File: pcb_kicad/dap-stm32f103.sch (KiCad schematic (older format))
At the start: 4 parts

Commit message: [update] pcb
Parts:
- added C?: 0402_100nF__104_10%_16V, lc_lib:0402_C, symbol lc_Cap:0402_100nF__104_10%_16V
- added R?: 0402_10KΩ__1002_1%, lc_lib:0402_R, symbol lc_RES:0402_10KΩ__1002_1%
- added R?: 0402_100KΩ__1003_1%, lc_lib:0402_R, symbol lc_RES:0402_100KΩ__1003_1%
- added R? (x2): 0402_4.7KΩ__4701_1%, lc_lib:0402_R, symbol lc_RES:0402_4.7KΩ__4701_1%
- added U? (x2): STM32F103CBT6, lc_lib:LQFP-48_7X7X05P, symbol lc_MCU:STM32F103CBT6
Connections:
- net labels added: +3.3V
- wire segments 9 -> 21
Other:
- moved on the sheet: C?, Y?

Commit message: [update] pcb sch
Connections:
- wire segments 21 -> 29
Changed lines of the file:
@@
 P 3800 2700
 F 0 "U?" H 3750 1111 50  0000 C CNN
-F 1 "STM32F103CBTx" H 3750 1020 50  0000 C CNN
+F 1 "STM32F103CBTx" H 3500 1000 50  0000 C CNN
 F 2 "Package_QFP:LQFP-48_7x7mm_P0.5mm" H 3200 1300 50  0001 R CNN
 F 3 "http://www.st.com/st-web-ui/static/active/en/resource/technical/document/datasheet/CD00161566.pdf" H 3800 2700 50  0001 C CNN
@@
 Wire Wire Line
 	5250 2950 5250 3050
+$Comp
+L power:GND #PWR?
+U 1 1 5D9F8DE0
+P 3900 4500
+F 0 "#PWR?" H 3900 4250 50  0001 C CNN
+F 1 "GND" H 3905 4327 50  0000 C CNN
+F 2 "" H 3900 4500 50  0001 C CNN
+F 3 "" H 3900 4500 50  0001 C CNN
+	1    3900 4500
+	1    0    0    -1
+$EndComp
+Wire Wire Line
+	3900 4500 3900 4200
+Wire Wire Line
+	3900 4200 3800 4200
+Connection ~ 3900 4200
+Connection ~ 3700 4200
+Wire Wire Line
+	3700 4200 3600 4200
+Connection ~ 3800 4200
+Wire Wire Line
+	3800 4200 3700 4200
+Wire Wire Line
+	3600 1200 3700 1200
+Connection ~ 3600 1200
+Connection ~ 3700 1200
+Wire Wire Line
+	3700 1200 3800 1200
+Connection ~ 3800 1200
+Wire Wire Line
+	3800 1200 3900 1200
+Connection ~ 3900 1200
+Wire Wire Line
+	3900 1200 4000 1200
 $EndSCHEMATC

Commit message: [update] SCH
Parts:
- removed U? (x2): STM32F103CBT6, lc_lib:LQFP-48_7X7X05P, symbol lc_MCU:STM32F103CBT6
- added C? (x2): 0402_18pF__180_5%_50V, lc_lib:0402_C, symbol lc_Cap:0402_18pF__180_5%_50V
- added C? (x2): 0402_100nF__104_10%_16V, lc_lib:0402_C, symbol lc_Cap:0402_100nF__104_10%_16V
- added C? (x2): 0603_10uF__106_10%_10V, lc_lib:0603_C, symbol lc_Cap:0603_10uF__106_10%_10V
- added D_BULE: 0603_蓝灯, lc_lib:0603_LED_S1, symbol lc_LED:0603_蓝灯
- added D_GREEN: 0603_绿灯, lc_lib:0603_LED_S1, symbol lc_LED:0603_绿灯
- added D_RED: 0603_红灯, lc_lib:0603_LED_S1, symbol lc_LED:0603_红灯
- added J?: USB_C_Receptacle_USB2.0, Connector_USB:USB_C_Receptacle_Palconn_UTC16-G, symbol Connector:USB_C_Receptacle_USB2.0
- added R? (x3): 0402_470Ω__4700_1%, lc_lib:0402_R, symbol lc_RES:0402_470Ω__4700_1%
- added R?: 0402_100Ω__1000_1%, lc_lib:0402_R, symbol lc_RES:0402_100Ω__1000_1%
- added R?: 0402_100KΩ__1003_1%, lc_lib:0402_R, symbol lc_RES:0402_100KΩ__1003_1%
- added R? (x2): 0402_33Ω__33R0_1%, lc_lib:0402_R, symbol lc_RES:0402_33Ω__33R0_1%
- added SWD/JTAG: Conn_02x05_Top_Bottom, Connector_PinHeader_2.54mm:PinHeader_2x05_P2.54mm_Vertical, symbol Connector_Generic:Conn_02x05_Top_Bottom
- added VR?: SOT-223_AMS1117-3.3, lc_lib:SOT-223, symbol lc_LDO:SOT-223_AMS1117-3.3
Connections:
- net labels added: LED_BULE, LED_GREEN, LED_RED, TGT_NRESET, TGT_RX, TGT_SWCLK, TGT_SWDIO, TGT_SWO, TGT_TX, TGT_USB_D+, TGT_USB_D-
- wire segments 29 -> 96
- no-connect marks 0 -> 5

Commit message: [update] SCH done
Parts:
- added C11, C12, C13, C14, C4: 0402_100nF__104_10%_16V, lc_lib:0402_C, symbol lc_Cap:0402_100nF__104_10%_16V
- added IF_SWD1: Conn_01x05, Connector_PinHeader_2.54mm:PinHeader_1x05_P2.54mm_Vertical, symbol Connector_Generic:Conn_01x05
- added R1: 0402_10KΩ__1002_1%, lc_lib:0402_R, symbol lc_RES:0402_10KΩ__1002_1%
- gave numbers to parts that had none: 24
- renumbered D_BULE to D_BULE1, D_GREEN to D_GREEN1, D_RED to D_RED1, SWD/JTAG to SWD/JTAG1
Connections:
- net +3V3: now also C11.1, C12.1, C13.1, C14.1, IF_SWD1.5 (Pin_5), R1.1
- net GND: now also U1.20 (PB2), C11.2, C12.2, C13.2, C14.2, C4.2, IF_SWD1.2 (Pin_2)
- net TGT_NRESET: now also U1.18 (PB0), C4.1, R1.2
- net TGT_RX: now also U1.12 (PA2)
- net IF_SWDIO: now reaches U1.34 (PA13)
- net IF_SWDIO: now also IF_SWD1.4 (Pin_4)
- net IF_SWCLK: now reaches U1.37 (PA14)
- net IF_SWCLK: now also IF_SWD1.3 (Pin_3)
- net IF_NRESET: now reaches C3.2, R8.2, U1.7 (NRST)
- net IF_NRESET: now also IF_SWD1.1 (Pin_1)
- no-connect marks 5 -> 22
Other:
- moved on the sheet: C3

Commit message: [update] pcb
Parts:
- added JTAG1: Conn_02x10_Top_Bottom, Connector_PinHeader_2.54mm:PinHeader_2x10_P2.54mm_Vertical, symbol Connector_Generic:Conn_02x10_Top_Bottom
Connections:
- net +3V3: now also JTAG1.1 (Pin_1), JTAG1.11 (Pin_11)
- net GND: now also JTAG1.12 (Pin_12), JTAG1.13 (Pin_13), JTAG1.14 (Pin_14), JTAG1.15 (Pin_15), JTAG1.16 (Pin_16), JTAG1.17 (Pin_17), JTAG1.18 (Pin_18), JTAG1.19 (Pin_19), JTAG1.20 (Pin_20)
- net TGT_NRESET: now also JTAG1.2 (Pin_2), JTAG1.8 (Pin_8)
- net TGT_RX: now also JTAG1.3 (Pin_3)
- net TGT_SWCLK: now also JTAG1.5 (Pin_5)
- net TGT_SWDIO: now also JTAG1.4 (Pin_4)
- net TGT_SWO: now also JTAG1.7 (Pin_7)
- no-connect marks 22 -> 25
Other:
- moved on the sheet: C11, C12, C13, C14, IF_SWD1, SWD/JTAG1

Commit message: [update] pcb 连线完成
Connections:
- net GND: now also J1.S1 (SHIELD)
- net TGT_NRESET: no longer JTAG1.2 (Pin_2)
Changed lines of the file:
@@
 NoConn ~ 4200 6750
 NoConn ~ 4200 6850
-NoConn ~ 3300 7150
 NoConn ~ 4200 5850
 NoConn ~ 4200 5950
@@
 Wire Wire Line
 	8800 4750 8850 4750
-Text Label 8400 4850 0    50   ~ 0
-TGT_NRESET
 Text Label 8400 4950 0    50   ~ 0
 TGT_RX
@@
 NoConn ~ 8850 5650
 Wire Wire Line
-	8400 4850 8850 4850
-Wire Wire Line
 	8400 4950 8850 4950
 Wire Wire Line
@@
 	8850 5450 8400 5450
 NoConn ~ 8850 5250
+NoConn ~ 8850 4850
+Wire Wire Line
+	3300 7150 3600 7150
+Connection ~ 3600 7150
 $EndSCHEMATC

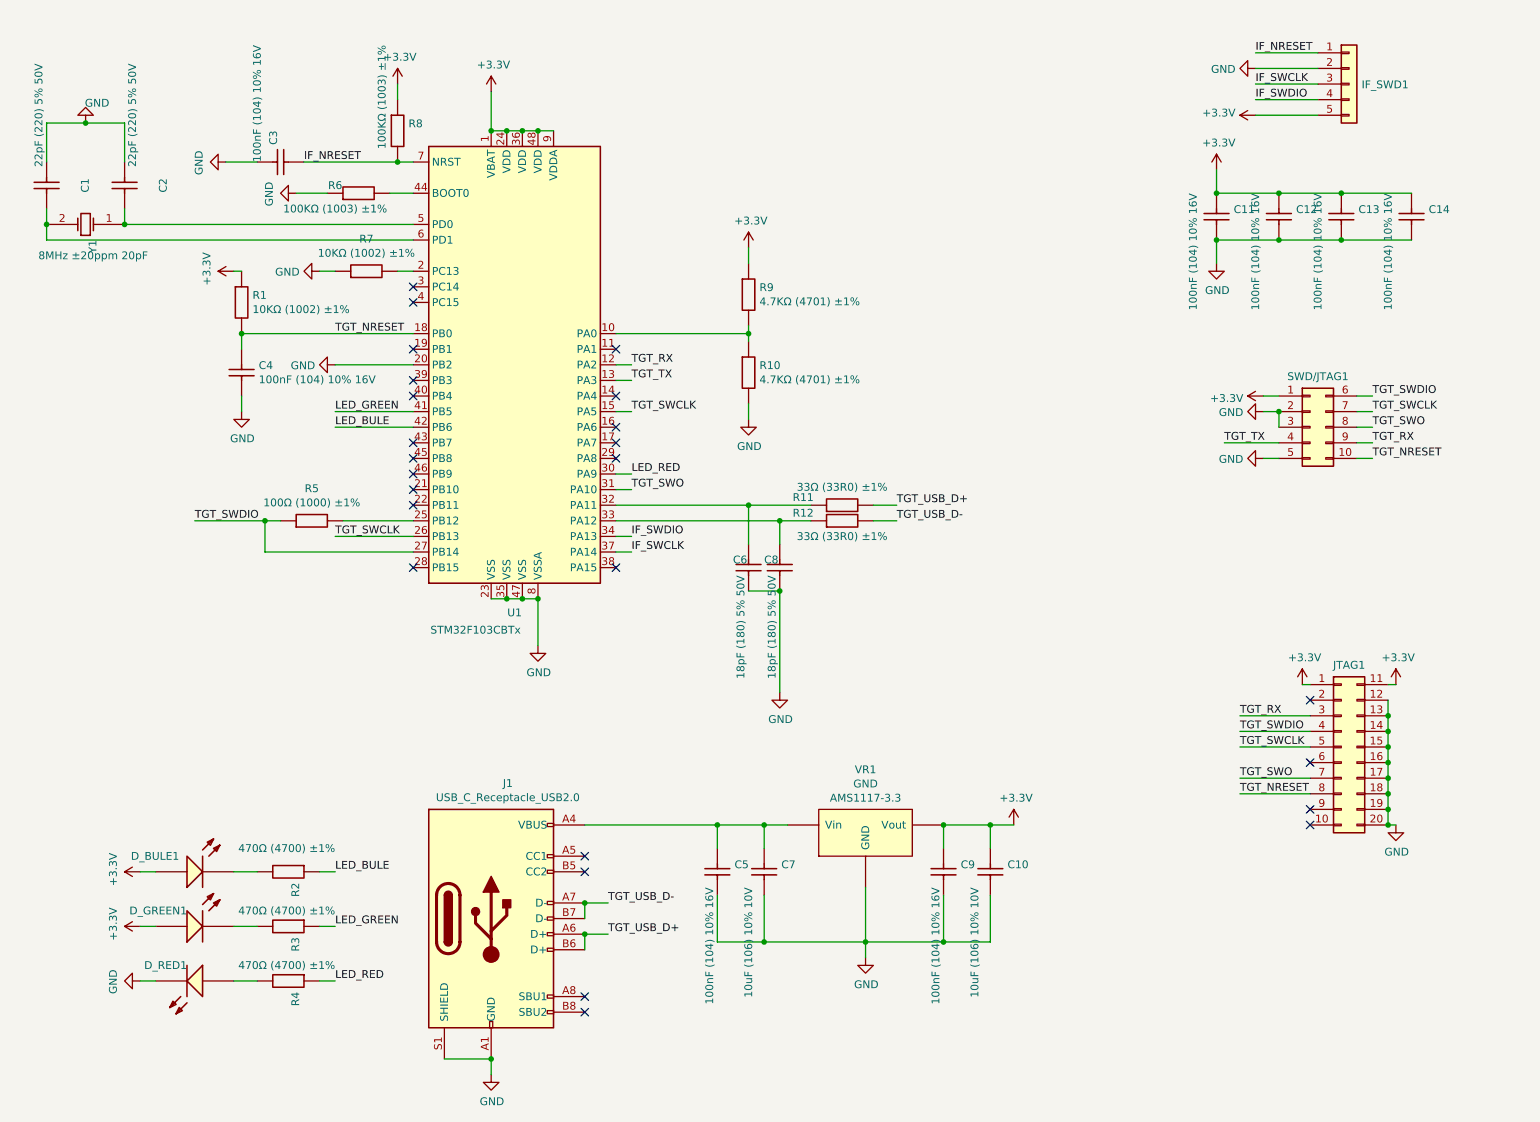
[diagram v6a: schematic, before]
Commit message: [update] stamp footprint
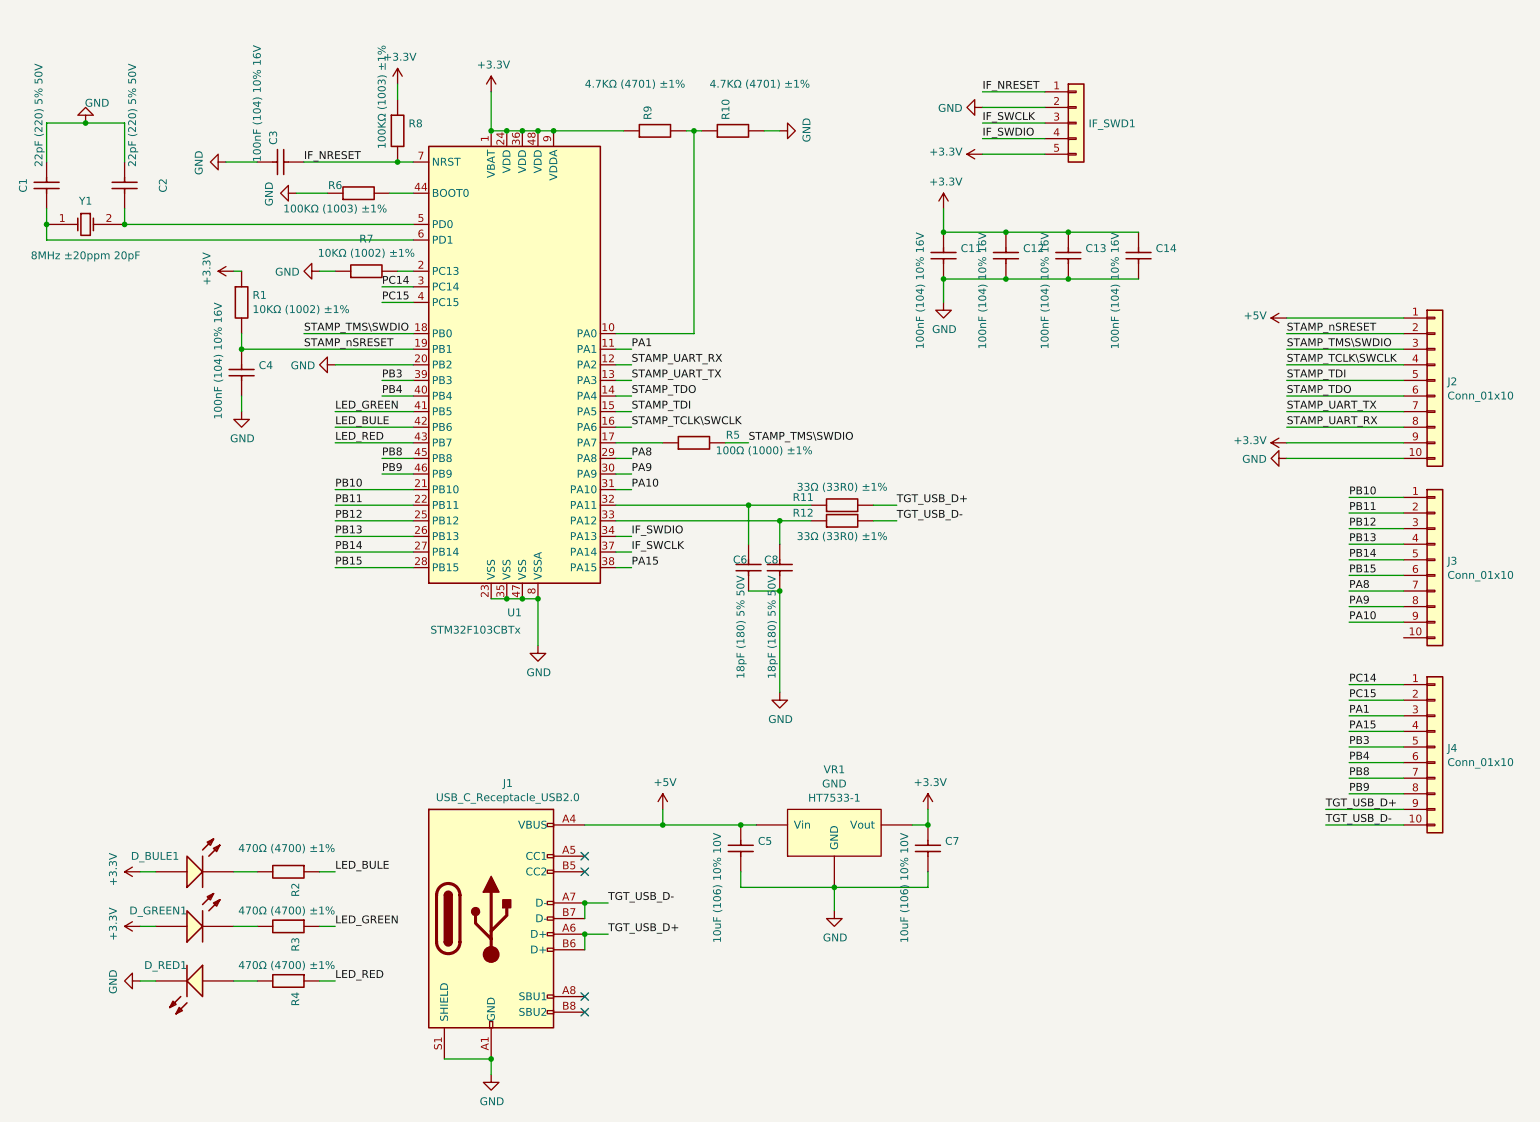
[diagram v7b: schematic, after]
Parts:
- removed C10: 0603_10uF__106_10%_10V, lc_lib:0603_C, symbol lc_Cap:0603_10uF__106_10%_10V
- removed C5, C9: 0402_100nF__104_10%_16V, lc_lib:0402_C, symbol lc_Cap:0402_100nF__104_10%_16V
- removed JTAG1: Conn_02x10_Top_Bottom, Connector_PinHeader_2.54mm:PinHeader_2x10_P2.54mm_Vertical, symbol Connector_Generic:Conn_02x10_Top_Bottom
- removed SWD/JTAG1: Conn_02x05_Top_Bottom, Connector_PinHeader_2.54mm:PinHeader_2x05_P2.54mm_Vertical, symbol Connector_Generic:Conn_02x05_Top_Bottom
- removed VR1: SOT-223_AMS1117-3.3, lc_lib:SOT-223, symbol lc_LDO:SOT-223_AMS1117-3.3
- added C5: 0603_10uF__106_10%_10V, lc_lib:0603_C, symbol lc_Cap:0603_10uF__106_10%_10V
- added J2, J3, J4: Conn_01x10, Connector_PinHeader_2.54mm:PinHeader_1x10_P2.54mm_Vertical, symbol Connector_Generic:Conn_01x10
- added VR1: SOT-89_HT7533-1, lc_lib:SOT-89(SOT-89-3), symbol lc_LDO:SOT-89_HT7533-1
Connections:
- net +3V3: now also C7.1, J2.9 (Pin_9), VR1.3 (Vout)
- net GND: now also C5.2, J2.10 (Pin_10), VR1.1 (GND)
- net LED_RED: now also U1.43 (PB7); no longer U1.30 (PA9)
- net TGT_USB_D+: now also J4.9 (Pin_9)
- net TGT_USB_D-: now also J4.10 (Pin_10)
- net PA1: now reaches U1.11 (PA1)
- net PA1: now also J4.3 (Pin_3)
- net STAMP_TDO: now reaches U1.14 (PA4)
- net STAMP_TDO: now also J2.6 (Pin_6)
- net STAMP_TCLK\SWCLK: now reaches U1.16 (PA6)
- net STAMP_TCLK\SWCLK: now also J2.4 (Pin_4)
- net at U1.17 (PA7): now also R5.1
- net STAMP_nSRESET: now reaches U1.19 (PB1)
- net STAMP_nSRESET: now also C4.1, R1.2, J2.2 (Pin_2)
- net PB10: now reaches U1.21 (PB10)
- net PB10: now also J3.1 (Pin_1)
- net PB11: now reaches U1.22 (PB11)
- net PB11: now also J3.2 (Pin_2)
- net PB12: now reaches U1.25 (PB12)
- net PB12: now also J3.3 (Pin_3); no longer R5.2
- net PB15: now reaches U1.28 (PB15)
- net PB15: now also J3.6 (Pin_6)
- net PA8: now reaches U1.29 (PA8)
- net PA8: now also J3.7 (Pin_7)
- net PC14: now reaches U1.3 (PC14)
- net PC14: now also J4.1 (Pin_1)
- net PA15: now reaches U1.38 (PA15)
- net PA15: now also J4.4 (Pin_4)
- net PB3: now reaches U1.39 (PB3)
- net PB3: now also J4.5 (Pin_5)
- net PC15: now reaches U1.4 (PC15)
- net PC15: now also J4.2 (Pin_2)
- net PB4: now reaches U1.40 (PB4)
- net PB4: now also J4.6 (Pin_6)
- net PB8: now reaches U1.45 (PB8)
- net PB8: now also J4.7 (Pin_7)
- net PB9: now reaches U1.46 (PB9)
- net PB9: now also J4.8 (Pin_8)
- net at C2.2, U1.5 (PD0): now also Y1.2 (OSC2); no longer Y1.1 (OSC1)
- net at C1.2, U1.6 (PD1): now also Y1.1 (OSC1); no longer Y1.2 (OSC2)
- net +5V: now reaches J1.A4 (VBUS), J1.A9 (VBUS), J1.B4 (VBUS), J1.B9 (VBUS)
- net +5V: now also C5.1, J2.1 (Pin_1), VR1.2 (Vin); no longer C7.1
- removed net TGT_NRESET: C4.1, R1.2, U1.18 (PB0)
- net TGT_RX renamed STAMP_UART_RX
- net STAMP_UART_RX: now also J2.8 (Pin_8)
- net TGT_SWCLK renamed PB13
- net PB13: now also J3.4 (Pin_4); no longer U1.15 (PA5)
- net TGT_SWDIO renamed PB14
- net PB14: now also J3.5 (Pin_5); no longer R5.1
- net TGT_SWO renamed PA10
- net PA10: now also J3.9 (Pin_9)
- net TGT_TX renamed STAMP_UART_TX
- net STAMP_UART_TX: now also J2.7 (Pin_7)
- new net PA9: J3.8 (Pin_8), U1.30 (PA9)
- new net STAMP_TDI: J2.5 (Pin_5), U1.15 (PA5)
- new net STAMP_TMS\SWDIO: J2.3 (Pin_3), R5.2, U1.18 (PB0)
- no-connect marks 25 -> 4
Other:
- moved on the sheet: C11, C12, C13, C14, IF_SWD1, R10, R9
